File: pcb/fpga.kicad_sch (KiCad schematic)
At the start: 45 parts, among them U1 XC7A50T-FTG256, U2 410-251-B, U3 S70KL1283GABHI020, U4 W25Q128JVS, Y1 ASE-20MHz

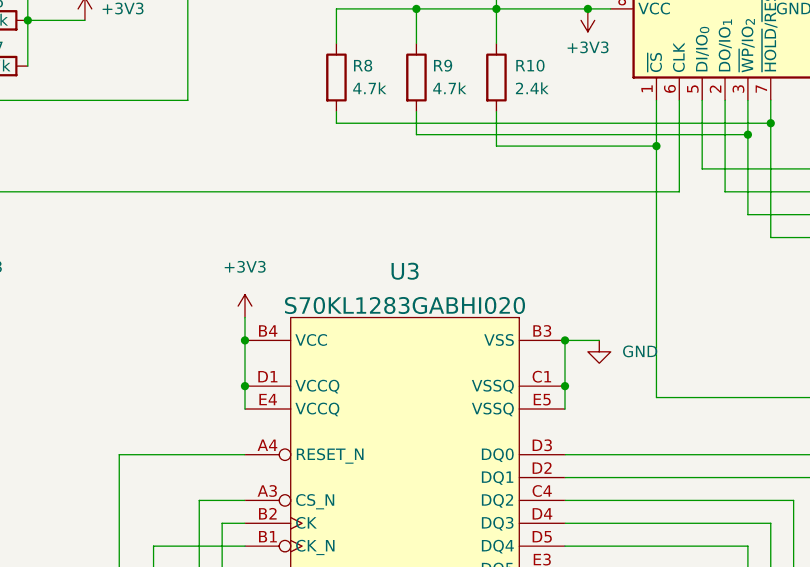
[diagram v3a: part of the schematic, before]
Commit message: pcb: change sram to dpb model
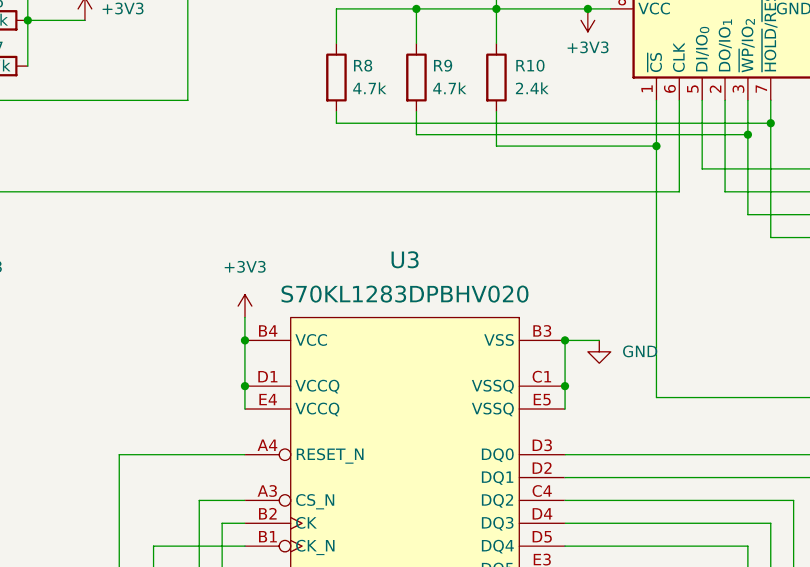
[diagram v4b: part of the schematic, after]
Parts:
- U3: value S70KL1283GABHI020 -> S70KL1283DPBHV020; symbol S70KL1283GABHI020:S70KL1283GABHI020 -> S70KL1283DPBHV020:S70KL1283DPBHV020; Manufacturer Order Number S70KL1283GABHI020 -> S70KL1283DPBHV020
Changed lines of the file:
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@@
 	)
 	(symbol
-		(lib_id "S70KL1283GABHI020:S70KL1283GABHI020")
+		(lib_id "S70KL1283DPBHV020:S70KL1283DPBHV020")
 		(at 152.4 88.9 0)
 		(unit 1)
@@
 		(fields_autoplaced yes)
 		(property "Reference" "U3"
-			(at 165.1 83.82 0)
+			(at 165.1 82.55 0)
 			(show_name no)
 			(do_not_autoplace no)
@@
 			)
 		)
-		(property "Value" "S70KL1283GABHI020"
-			(at 165.1 87.63 0)
+		(property "Value" "S70KL1283DPBHV020"
+			(at 165.1 86.36 0)
 			(show_name no)
 			(do_not_autoplace no)
@@
 			)
 		)
-		(property "Manufacturer Order Number" "S70KL1283GABHI020"
+		(property "Manufacturer Order Number" "S70KL1283DPBHV020"
 			(at 146.812 109.474 0)
 			(hide yes)
